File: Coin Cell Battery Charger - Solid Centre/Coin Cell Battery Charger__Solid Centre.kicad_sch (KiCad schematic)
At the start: 52 parts, among them J1 0473461001, J4 UJ2-MIBV-4-SMT-TR-67, Q2 Q_PMOS_GSD, SW1 5136TR, U1 BQ21040DBVR, U2 TLV74010PDBVR, U3 LTC6992CS6-3#TRMPBF, U4 AP2502KTR-G1, U5 AP2502KTR-G1, U6 LTC2954CTS8-1#TRMPBF

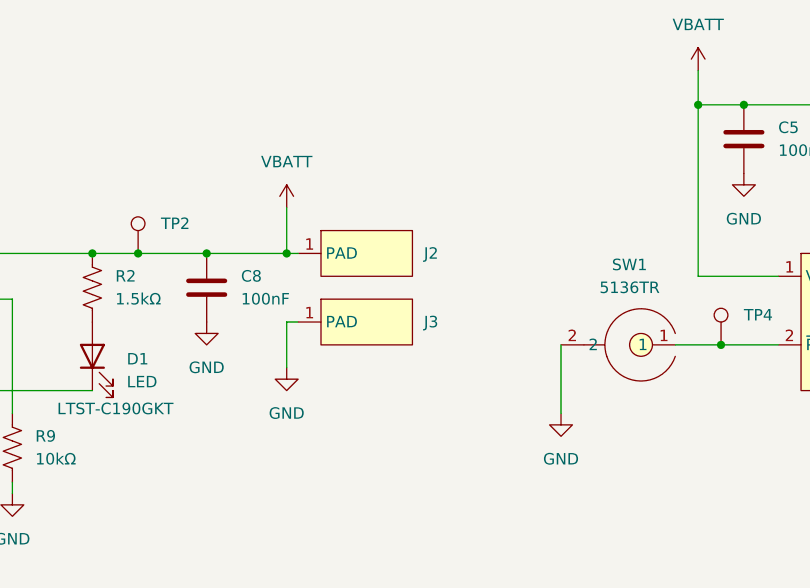
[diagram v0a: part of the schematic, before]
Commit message: Battery Holder additions
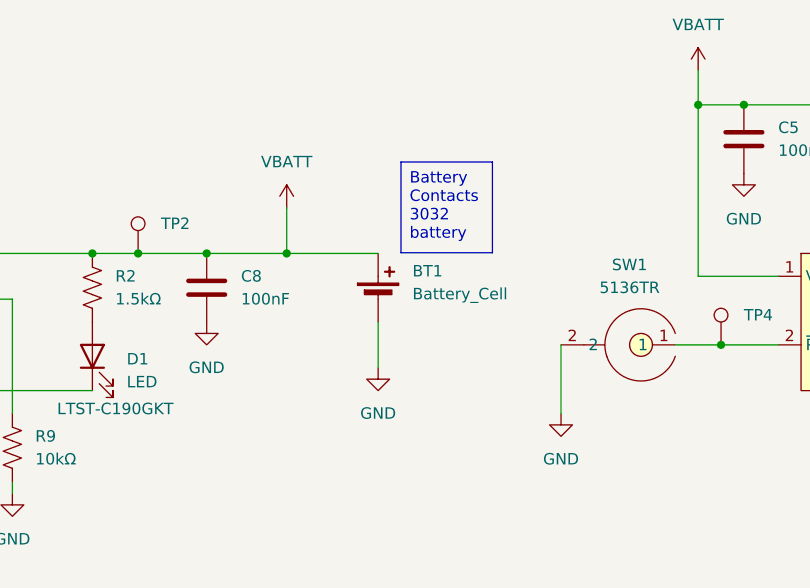
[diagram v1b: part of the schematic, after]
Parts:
- removed J2, J3: (no value), _Dylan_IC:Solder_Pad_0.6mmx2mm, symbol Dylan Components:Solder_Pad_0.6mmx2mm
- added BT1: Battery_Cell, symbol Device:Battery_Cell
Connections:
- net GND: now also BT1.2 (-)
- net VBATT: now also BT1.1 (+)
